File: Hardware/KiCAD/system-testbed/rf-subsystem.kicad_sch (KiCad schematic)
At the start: 34 parts, among them P1 SMA, U2 SKY13278-313, U3 CC1200RHBR, U4 SKY13278-313, U5 SKY13278-313, U6 SKY13278-313, U7 SKY13278-313, U8 SKY13278-313, U9 SN74LVC2G14DBV, X3 40 MHz, X4 EYE_SPI_DISPLAY_FLIP

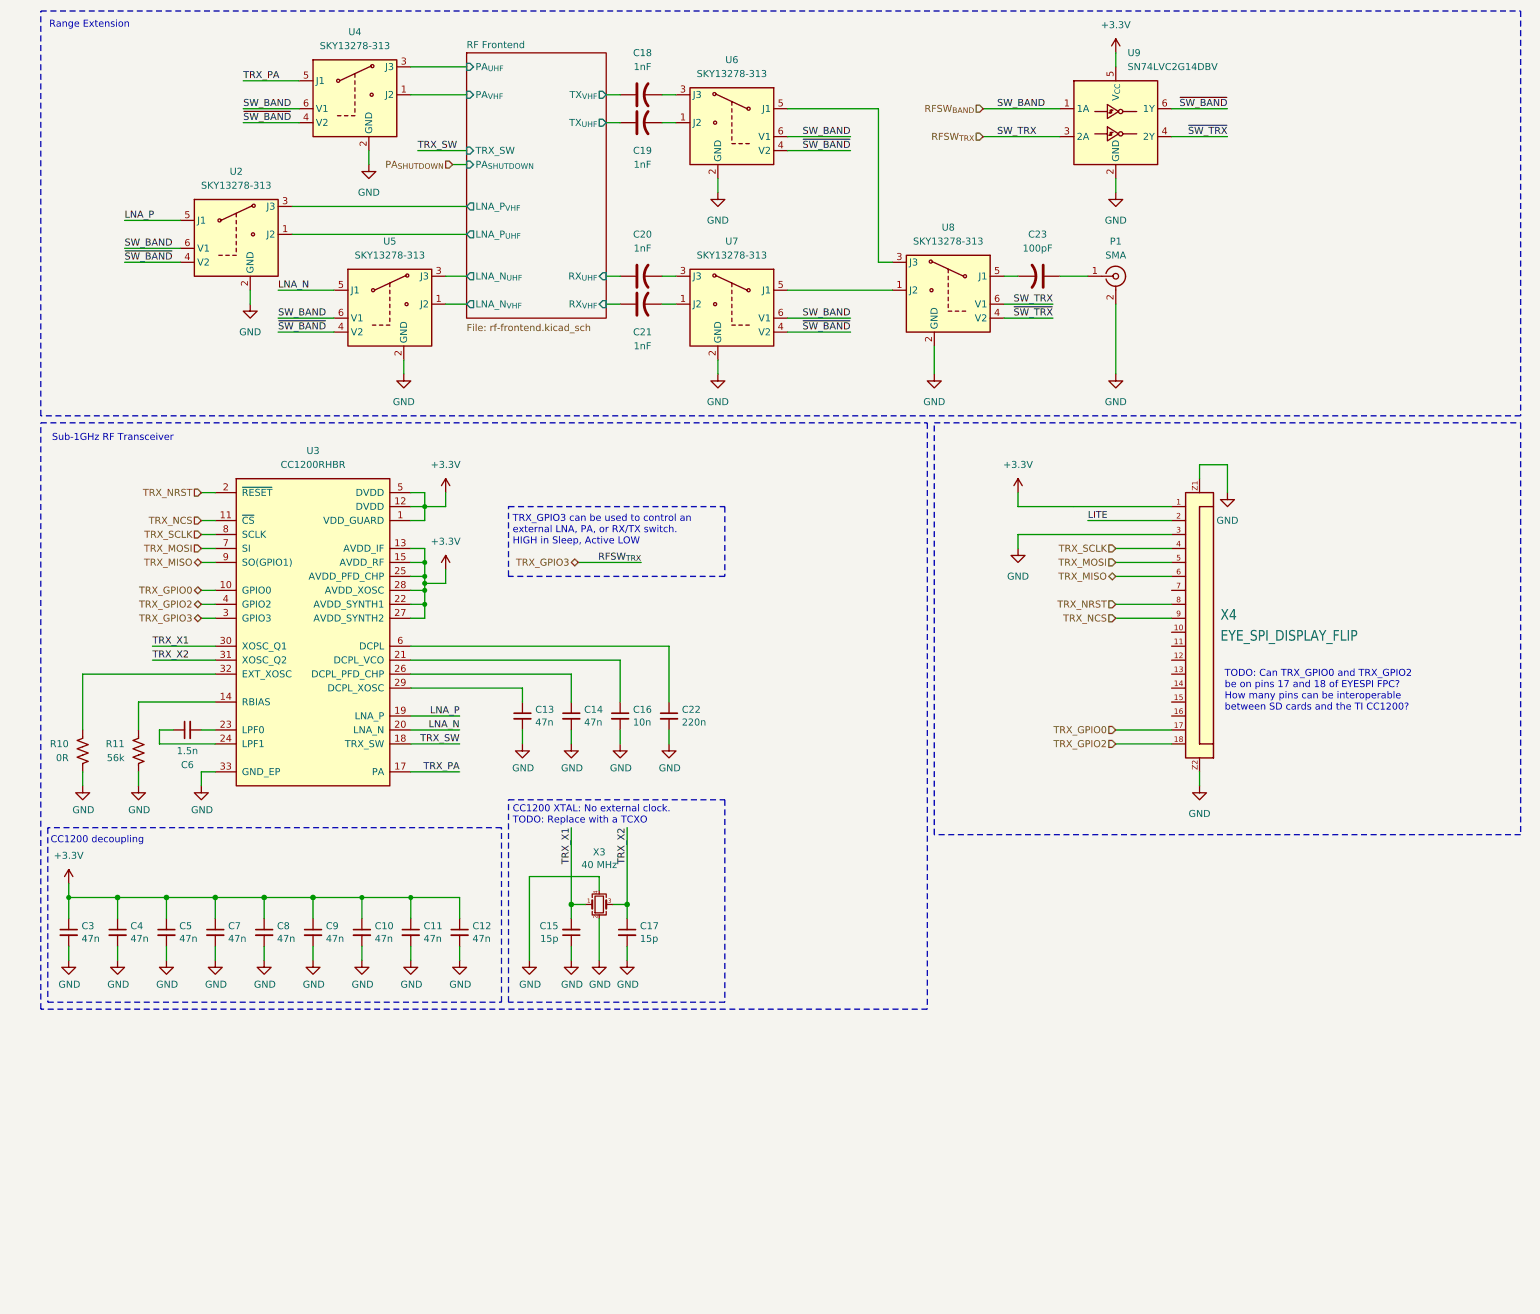
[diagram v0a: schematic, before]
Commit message: fix: import RF sheet contents #65
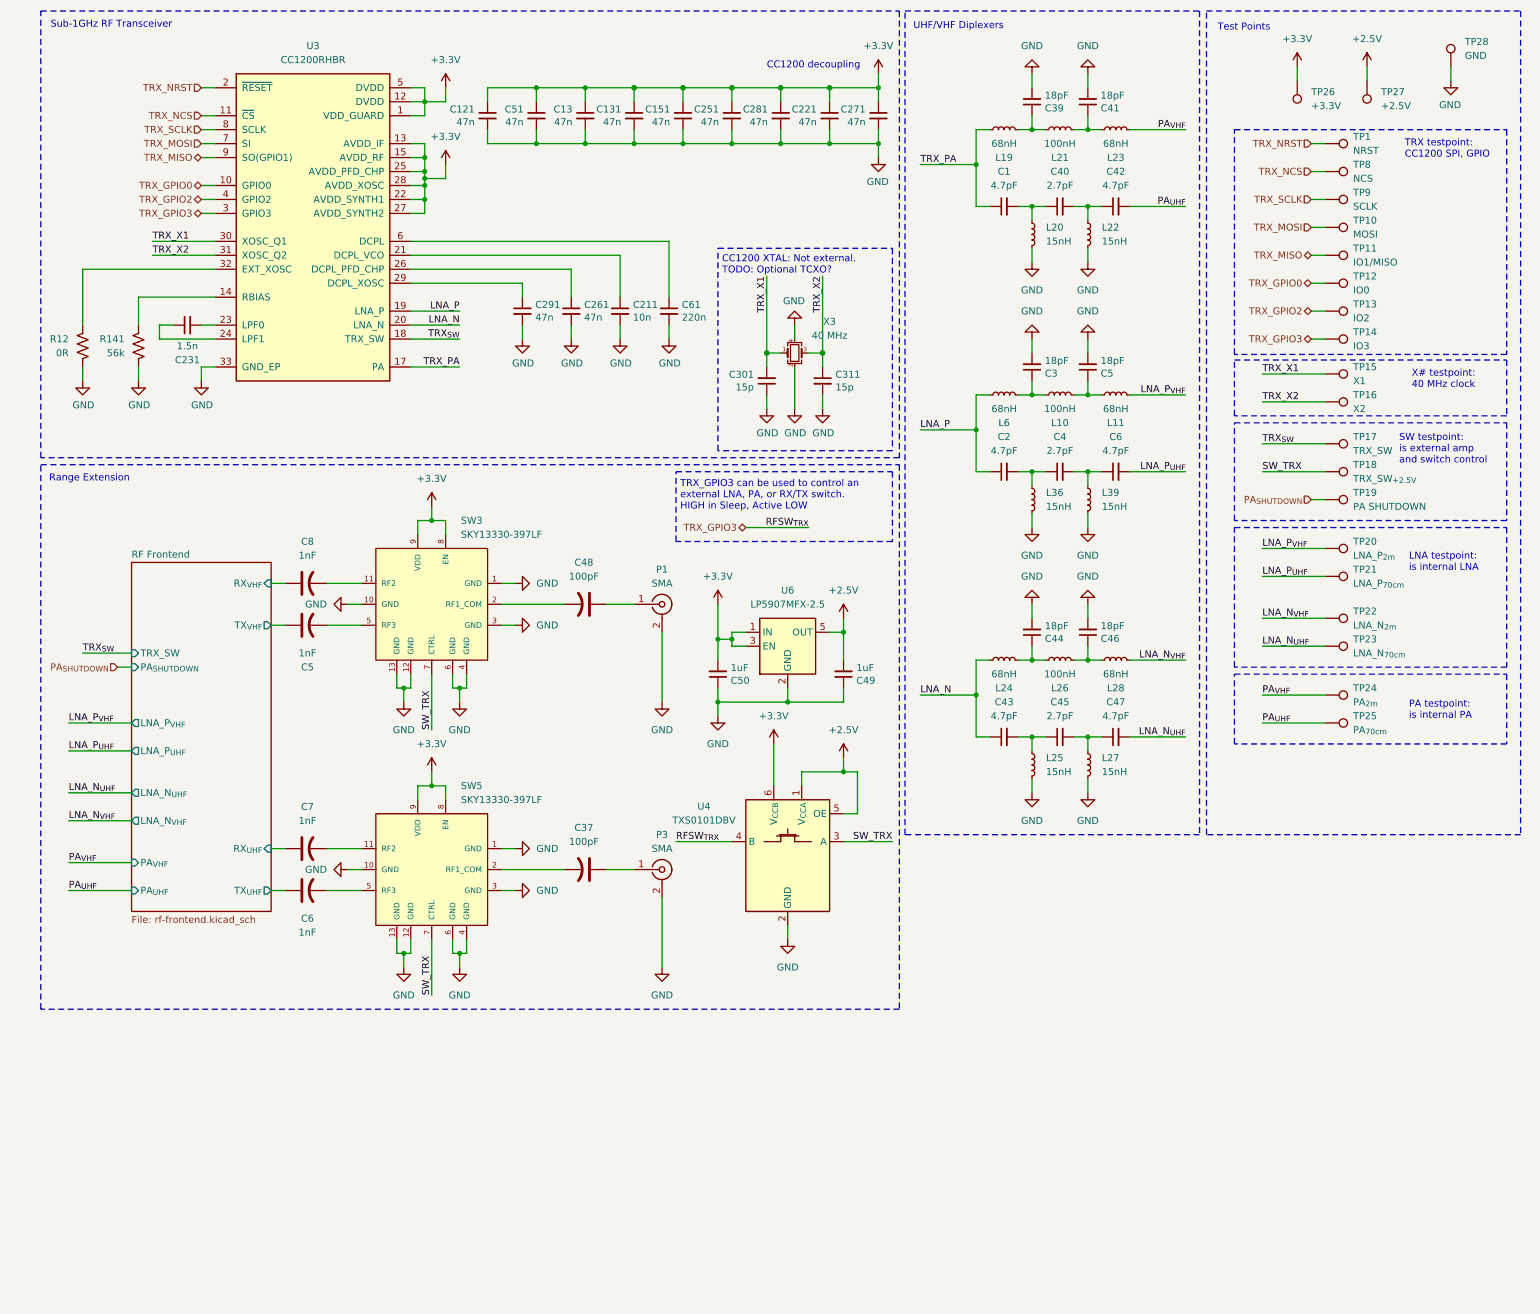
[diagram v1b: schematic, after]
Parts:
- removed U2, U4, U5, U6, U7, U8: SKY13278-313, symbol capstone-project:SKY13278-313
- removed U9: SN74LVC2G14DBV, Package_TO_SOT_SMD:SOT-23-6, symbol 74xGxx:SN74LVC2G14DBV
- removed X4: EYE_SPI_DISPLAY_FLIP, capstone-project:Adafruit EYESPI FPC Connector, symbol capstone-project:Adafruit EYESPI FPC Connector
- added C1, C2, C42, C43, C47, C6: 4.7pF, symbol Device:C_Small
- added C3, C39, C41, C44, C46, C5: 18pF, Capacitor_SMD:C_0603_1608Metric, symbol Device:C_Small
- added C4, C40, C45: 2.7pF, symbol Device:C_Small
- added C48: 100pF, Capacitor_SMD:C_0603_1608Metric, symbol Device:C_US
- added C49, C50: 1uF, Capacitor_SMD:C_0603_1608Metric, symbol Device:C_Small
- added L10, L21, L26: 100nH, symbol Device:L_Small
- added L11, L19, L23, L24, L28, L6: 68nH, symbol Device:L_Small
- added L20, L22, L25, L27, L36, L39: 15nH, Capacitor_SMD:C_0603_1608Metric, symbol Device:L_Small
- added P1: SMA, Connector_Coaxial:SMA_Amphenol_901-143_Horizontal, symbol Connector:Conn_Coaxial
- added SW3, SW5: SKY13330-397LF, SKY13330-397LF:SKY13330-397LF, symbol capstone-project:SKY13330-397LF
- added TP1: NRST, symbol Connector:TestPoint
- added TP10: MOSI, symbol Connector:TestPoint
- added TP11: IO1/MISO, symbol Connector:TestPoint
- added TP12: IO0, symbol Connector:TestPoint
- added TP13: IO2, symbol Connector:TestPoint
- added TP14: IO3, symbol Connector:TestPoint
- added TP15: X1, symbol Connector:TestPoint
- added TP16: X2, symbol Connector:TestPoint
- added TP17: TRX_SW, symbol Connector:TestPoint
- added TP18: TRX_SW_{+2.5V}, symbol Connector:TestPoint
- added TP19: PA SHUTDOWN, symbol Connector:TestPoint
- added TP20: LNA_P_{2m}, symbol Connector:TestPoint
- added TP21: LNA_P_{70cm}, symbol Connector:TestPoint
- added TP22: LNA_N_{2m}, symbol Connector:TestPoint
- added TP23: LNA_N_{70cm}, symbol Connector:TestPoint
- added TP24: PA_{2m}, symbol Connector:TestPoint
- added TP25: PA_{70cm}, symbol Connector:TestPoint
- added TP26: +3.3V, symbol Connector:TestPoint
- added TP27: +2.5V, symbol Connector:TestPoint
- added TP28: GND, symbol Connector:TestPoint
- added TP8: NCS, symbol Connector:TestPoint
- added TP9: SCLK, symbol Connector:TestPoint
- added U4: TXS0101DBV, Package_TO_SOT_SMD:SOT-23-6, symbol Logic_LevelTranslator:TXS0101DBV
- added U6: LP5907MFX-2.5, Package_TO_SOT_SMD:SOT-23-5, symbol Regulator_Linear:LP5907MFX-2.5
- renumbered C12 to C121, C10 to C13, C9 to C131, C8 to C151, C16 to C211, C4 to C221, C6 to C231, C7 to C251, C14 to C261, C3 to C271, C5 to C281, C13 to C291, C15 to C301, C17 to C311, C23 to C37, C18 to C5, C11 to C51, C19 to C6, C22 to C61, C20 to C7, C21 to C8, P1 to P3, R10 to R12, R11 to R141
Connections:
- net +3.3V: now also C50.2, SW3.8 (EN), SW3.9 (VDD), SW5.8 (EN), SW5.9 (VDD), TP26.1, U4.6 (V_{CCB}), U6.1 (IN), U6.3 (EN)
- net GND: now also C3.2, C39.2, C41.2, C44.2, C46.2, C49.1, C5.2, C50.1, L20.2, L22.2, L25.2, L27.2, L36.2, L39.2, P1.2 (Ext), SW3.1 (GND), SW3.10 (GND), SW3.12 (GND), SW3.13 (GND), SW3.3 (GND), SW3.4 (GND), SW3.6 (GND), SW5.1 (GND), SW5.10 (GND), SW5.12 (GND), SW5.13 (GND), SW5.3 (GND), SW5.4 (GND), SW5.6 (GND), TP28.1, U4.2 (GND), U6.2 (GND)
- net LNA_N: now also C43.1, L24.1
- net LNA_P: now also C2.1, L6.1
- net PA_{SHUTDOWN}: now also TP19.1
- net TRX_GPIO0: now also TP12.1
- net TRX_GPIO2: now also TP13.1
- net TRX_MISO: now also TP11.1
- net TRX_MOSI: now also TP10.1
- net TRX_NCS: now also TP8.1
- net TRX_NRST: now also TP1.1
- net TRX_PA: now also C1.1, L19.1
- net TRX_SCLK: now also TP9.1
- net TRX_X1: now also TP15.1
- net TRX_X2: now also TP16.1
- net at C37.2: now also SW5.2 (RF1_COM)
- net at C5.2: now also SW3.5 (RF3)
- net at C8.2: now also SW3.11 (RF2)
- net at C6.2: now also SW5.5 (RF3)
- net at C7.2: now also SW5.11 (RF2)
- net RFSW_{TRX} renamed TRX_GPIO3
- net TRX_GPIO3: now also TP14.1, U4.4 (B)
- net TRX_SW renamed TRX_{SW}
- net TRX_{SW}: now also TP17.1
- new net: C44.1, L24.2, L26.1
- new net: C1.2, C40.1, L20.1
- new net: C48.2, SW3.2 (RF1_COM)
- new net: C40.2, C42.1, L22.1
- new net: C48.1, P1.1 (In)
- new net: C45.2, C47.1, L27.1
- new net: C41.1, L21.2, L23.1
- new net: C5.1, L10.2, L11.1
- new net: C2.2, C4.1, L36.1
- new net: C39.1, L19.2, L21.1
- new net: C43.2, C45.1, L25.1
- new net: C4.2, C6.1, L39.1
- new net: C3.1, L10.1, L6.2
- new net: C46.1, L26.2, L28.1
- new net +2.5V: C49.2, TP27.1, U4.1 (V_{CCA}), U4.5 (OE), U6.5 (OUT)
- new net LNA_N_{UHF}: C47.2, TP23.1
- new net LNA_N_{VHF}: L28.2, TP22.1
- new net LNA_P_{UHF}: C6.2, TP21.1
- new net LNA_P_{VHF}: L11.2, TP20.1
- new net PA_{UHF}: C42.2, TP25.1
- new net PA_{VHF}: L23.2, TP24.1
- new net SW_TRX: SW3.7 (CTRL), SW5.7 (CTRL), TP18.1, U4.3 (A)
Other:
- note added: "CC1200 XTAL: Not external. TODO: Optional TCXO?"
- note added: "LNA testpoint: is internal LNA"
- note added: "PA testpoint: is internal PA"
- note added: "SW testpoint: is external amp and switch control"
- note added: "TRX testpoint: CC1200 SPI, GPIO"
- note added: "Test Points"
- note added: "UHF/VHF Diplexers"
- note added: "X# testpoint: 40 MHz clock"
- note removed: "CC1200 XTAL: No external clock. TODO: Replace with a TCXO"
- note removed: "TODO: Can TRX_GPIO0 and TRX_GPIO2 be on pins 17 and 18 of EYESPI FPC? How many pins can be interoperable between SD cards and the TI CC1200?"
- moved on the sheet: C121, C13, C131, C151, C211, C221, C231, C251, C261, C271, C281, C291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

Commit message: fix: begin reannotations #65 #70
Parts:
- renumbered C8 to C, L23 to L?, L19 to L?, L11 to L?, L10 to L?
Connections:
- net LNA_P_{VHF}: now also L?.1; no longer L?.2
- net at C5.1, L?.2: now also L?.2; no longer L?.1
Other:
- moved on the sheet: L?
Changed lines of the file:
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@@
 	)
 	(rectangle
+		(start 502.92 -72.39)
+		(end 502.92 -72.39)
+		(stroke
+			(width 0)
+			(type default)
+		)
+		(fill
+			(type none)
+		)
+	)
+	(rectangle
 		(start 137.16 57.15)
 		(end 168.91 93.98)
@@
 		(on_board yes)
 		(dnp no)
-		(property "Reference" "#PWR044"
+		(property "Reference" "#PWR0108"
 			(at 146.05 92.71 0)
 			(effects
@@
 			(project "system-testbed"
 				(path "/72756aea-0ff9-4757-9699-8d0f18588f6f/663959ae-8fbf-4d79-b07e-771da73defb9"
-					(reference "#PWR044")
+					(reference "#PWR0108")
 					(unit 1)
 				)
@@
 		(dnp no)
 		(fields_autoplaced yes)
-		(property "Reference" "#PWR036"
+		(property "Reference" "#PWR0125"
 			(at 63.5 121.92 0)
 			(effects
@@
 			(project "system-testbed"
 				(path "/72756aea-0ff9-4757-9699-8d0f18588f6f/663959ae-8fbf-4d79-b07e-771da73defb9"
-					(reference "#PWR036")
+					(reference "#PWR0125")
 					(unit 1)
 				)
@@
 		(on_board yes)
 		(dnp no)
-		(property "Reference" "#PWR047"
+		(property "Reference" "#PWR0109"
 			(at 156.21 92.71 0)
 			(effects
@@
 			(project "system-testbed"
 				(path "/72756aea-0ff9-4757-9699-8d0f18588f6f/663959ae-8fbf-4d79-b07e-771da73defb9"
-					(reference "#PWR047")
+					(reference "#PWR0109")
 					(unit 1)
 				)
@@
 		(dnp no)
 		(fields_autoplaced yes)
-		(property "Reference" "#PWR041"
+		(property "Reference" "#PWR0128"
 			(at 149.86 189.23 0)
 			(effects
@@
 			(project "system-testbed"
 				(path "/72756aea-0ff9-4757-9699-8d0f18588f6f/663959ae-8fbf-4d79-b07e-771da73defb9"
-					(reference "#PWR041")
+					(reference "#PWR0128")
 					(unit 1)
 				)
@@
 		(on_board yes)
 		(dnp no)
-		(property "Reference" "#PWR048"
+		(property "Reference" "#PWR0118"
 			(at 128.27 80.01 0)
 			(effects
@@
 			(project "system-testbed"
 				(path "/72756aea-0ff9-4757-9699-8d0f18588f6f/663959ae-8fbf-4d79-b07e-771da73defb9"
-					(reference "#PWR048")
+					(reference "#PWR0118")
 					(unit 1)
 				)
@@
 		(on_board yes)
 		(dnp no)
-		(property "Reference" "#PWR043"
+		(property "Reference" "#PWR0119"
 			(at 166.37 46.99 0)
 			(effects
@@
 			(project "system-testbed"
 				(path "/72756aea-0ff9-4757-9699-8d0f18588f6f/663959ae-8fbf-4d79-b07e-771da73defb9"
-					(reference "#PWR043")
+					(reference "#PWR0119")
 					(unit 1)
 				)
@@
 		(on_board yes)
 		(dnp no)
-		(fields_autoplaced yes)
-		(property "Reference" "L23"
+		(property "Reference" "L?"
 			(at 209.55 40.64 90)
 			(effects
@@
 			(project "system-testbed"
 				(path "/72756aea-0ff9-4757-9699-8d0f18588f6f/663959ae-8fbf-4d79-b07e-771da73defb9"
-					(reference "L23")
+					(reference "L?")
 					(unit 1)
 				)
@@
 		(dnp no)
 		(fields_autoplaced yes)
-		(property "Reference" "#PWR039"
+		(property "Reference" "#PWR0126"
 			(at 137.16 125.73 0)
 			(effects
@@
 			(project "system-testbed"
 				(path "/72756aea-0ff9-4757-9699-8d0f18588f6f/663959ae-8fbf-4d79-b07e-771da73defb9"
-					(reference "#PWR039")
+					(reference "#PWR0126")
 					(unit 1)
 				)
@@
 		(dnp no)
 		(fields_autoplaced yes)
-		(property "Reference" "#PWR035"
+		(property "Reference" "#PWR0127"
 			(at 106.68 118.11 0)
 			(effects
@@
 			(project "system-testbed"
 				(path "/72756aea-0ff9-4757-9699-8d0f18588f6f/663959ae-8fbf-4d79-b07e-771da73defb9"
-					(reference "#PWR035")
+					(reference "#PWR0127")
 					(unit 1)
 				)
@@
 		(dnp no)
 		(fields_autoplaced yes)
-		(property "Reference" "#PWR042"
+		(property "Reference" "#PWR0113"
 			(at 166.37 29.21 0)
 			(effects
@@
 			(project "system-testbed"
 				(path "/72756aea-0ff9-4757-9699-8d0f18588f6f/663959ae-8fbf-4d79-b07e-771da73defb9"
-					(reference "#PWR042")
+					(reference "#PWR0113")
 					(unit 1)
 				)
@@
 		(on_board yes)
 		(dnp no)
-		(property "Reference" "#PWR031"
+		(property "Reference" "#PWR0112"
 			(at 21.59 87.63 0)
 			(effects
@@
 			(project "system-testbed"
 				(path "/72756aea-0ff9-4757-9699-8d0f18588f6f/663959ae-8fbf-4d79-b07e-771da73defb9"
-					(reference "#PWR031")
+					(reference "#PWR0112")
 					(unit 1)
 				)
@@
 		(on_board yes)
 		(dnp no)
-		(property "Reference" "#PWR045"
+		(property "Reference" "#PWR0110"
 			(at 151.13 92.71 0)
 			(effects
@@
 			(project "system-testbed"
 				(path "/72756aea-0ff9-4757-9699-8d0f18588f6f/663959ae-8fbf-4d79-b07e-771da73defb9"
-					(reference "#PWR045")
+					(reference "#PWR0110")
 					(unit 1)
 				)
@@
 		(on_board yes)
 		(dnp no)
-		(property "Reference" "#PWR040"
+		(property "Reference" "#PWR0123"
 			(at 80.01 146.05 0)
 			(effects
@@
 			(project "system-testbed"
 				(path "/72756aea-0ff9-4757-9699-8d0f18588f6f/663959ae-8fbf-4d79-b07e-771da73defb9"
-					(reference "#PWR040")
+					(reference "#PWR0123")
 					(unit 1)
 				)
@@
 		(dnp no)
 		(fields_autoplaced yes)
-		(property "Reference" "#PWR057"
+		(property "Reference" "#PWR0120"
 			(at 127 194.31 0)
 			(effects
@@
 			(project "system-testbed"
 				(path "/72756aea-0ff9-4757-9699-8d0f18588f6f/663959ae-8fbf-4d79-b07e-771da73defb9"
-					(reference "#PWR057")
+					(reference "#PWR0120")
 					(unit 1)
 				)
@@
 		(dnp no)
 		(fields_autoplaced yes)
-		(property "Reference" "C8"
+		(property "Reference" "C"
 			(at 62.484 110.49 90)
 			(effects
@@
 			(project "system-testbed"
 				(path "/72756aea-0ff9-4757-9699-8d0f18588f6f/663959ae-8fbf-4d79-b07e-771da73defb9"
-					(reference "C8")
+					(reference "C")
 					(unit 1)
 				)
@@
 		(on_board yes)
 		(dnp no)
-		(property "Reference" "#PWR046"
+		(property "Reference" "#PWR0111"
 			(at 119.38 80.01 0)
 			(effects
@@
 			(project "system-testbed"
 				(path "/72756aea-0ff9-4757-9699-8d0f18588f6f/663959ae-8fbf-4d79-b07e-771da73defb9"
-					(reference "#PWR046")
+					(reference "#PWR0111")
 					(unit 1)
 				)
@@
 		(dnp no)
 		(fields_autoplaced yes)
-		(property "Reference" "#PWR065"
+		(property "Reference" "#PWR0122"
 			(at 63.5 170.18 0)
 			(effects
@@
 			(project "system-testbed"
 				(path "/72756aea-0ff9-4757-9699-8d0f18588f6f/663959ae-8fbf-4d79-b07e-771da73defb9"
-					(reference "#PWR065")
+					(reference "#PWR0122")
 					(unit 1)
 				)
@@
 		(on_board yes)
 		(dnp no)
-		(fields_autoplaced yes)
-		(property "Reference" "L19"
+		(property "Reference" "L?"
 			(at 189.23 40.64 90)
 			(effects
@@
 			(project "system-testbed"
 				(path "/72756aea-0ff9-4757-9699-8d0f18588f6f/663959ae-8fbf-4d79-b07e-771da73defb9"
-					(reference "L19")
+					(reference "L?")
 					(unit 1)
 				)
@@
 		(dnp no)
 		(fields_autoplaced yes)
-		(property "Reference" "#PWR038"
+		(property "Reference" "#PWR0124"
 			(at 85.09 156.21 0)
 			(effects
@@
 			(project "system-testbed"
 				(path "/72756aea-0ff9-4757-9699-8d0f18588f6f/663959ae-8fbf-4d79-b07e-771da73defb9"
-					(reference "#PWR038")
+					(reference "#PWR0124")
 					(unit 1)
 				)
@@
 		(dnp no)
 		(fields_autoplaced yes)
-		(property "Reference" "#PWR037"
+		(property "Reference" "#PWR0121"
 			(at 127 146.05 0)
 			(effects
@@
 			(project "system-testbed"
 				(path "/72756aea-0ff9-4757-9699-8d0f18588f6f/663959ae-8fbf-4d79-b07e-771da73defb9"
-					(reference "#PWR037")
+					(reference "#PWR0121")
 					(unit 1)
 				)
@@
 	(symbol
 		(lib_id "Device:L_Small")
-		(at 209.55 83.82 90)
+		(at 209.55 83.82 270)
+		(mirror x)
 		(unit 1)
 		(exclude_from_sim no)
@@
 		(on_board yes)
 		(dnp no)
-		(fields_autoplaced yes)
-		(property "Reference" "L11"
+		(property "Reference" "L?"
 			(at 209.55 88.9 90)
 			(effects
@@
 			(project "system-testbed"
 				(path "/72756aea-0ff9-4757-9699-8d0f18588f6f/663959ae-8fbf-4d79-b07e-771da73defb9"
-					(reference "L11")
+					(reference "L?")
 					(unit 1)
 				)
@@
 		(on_board yes)
 		(dnp no)
-		(fields_autoplaced yes)
-		(property "Reference" "L10"
+		(property "Reference" "L?"
 			(at 199.39 88.9 90)
 			(effects
@@
 			(project "system-testbed"
 				(path "/72756aea-0ff9-4757-9699-8d0f18588f6f/663959ae-8fbf-4d79-b07e-771da73defb9"
-					(reference "L10")
+					(reference "L?")
 					(unit 1)
 				)
